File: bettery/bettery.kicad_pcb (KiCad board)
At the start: 2 copper layers, 72.2 x 45.2 mm, 61 parts, among them J2 Conn_01x10_Socket, J4 Conn_ARM_SWD_TagConnect_TC2030, Q1 WMB014N06LG4, Q2 WMB014N06LG4, U1 L9961, U2 STM32G070KBTx

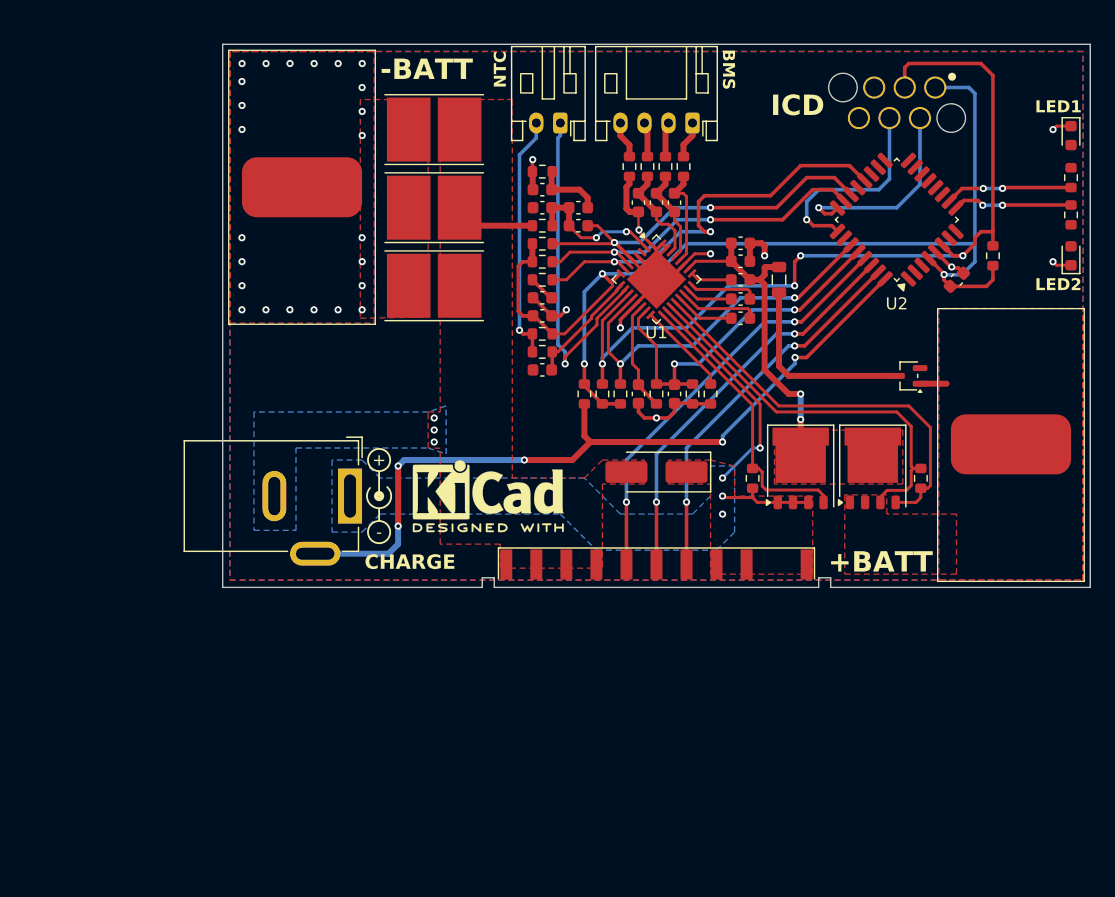
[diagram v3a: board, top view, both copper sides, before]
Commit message: add chassis models
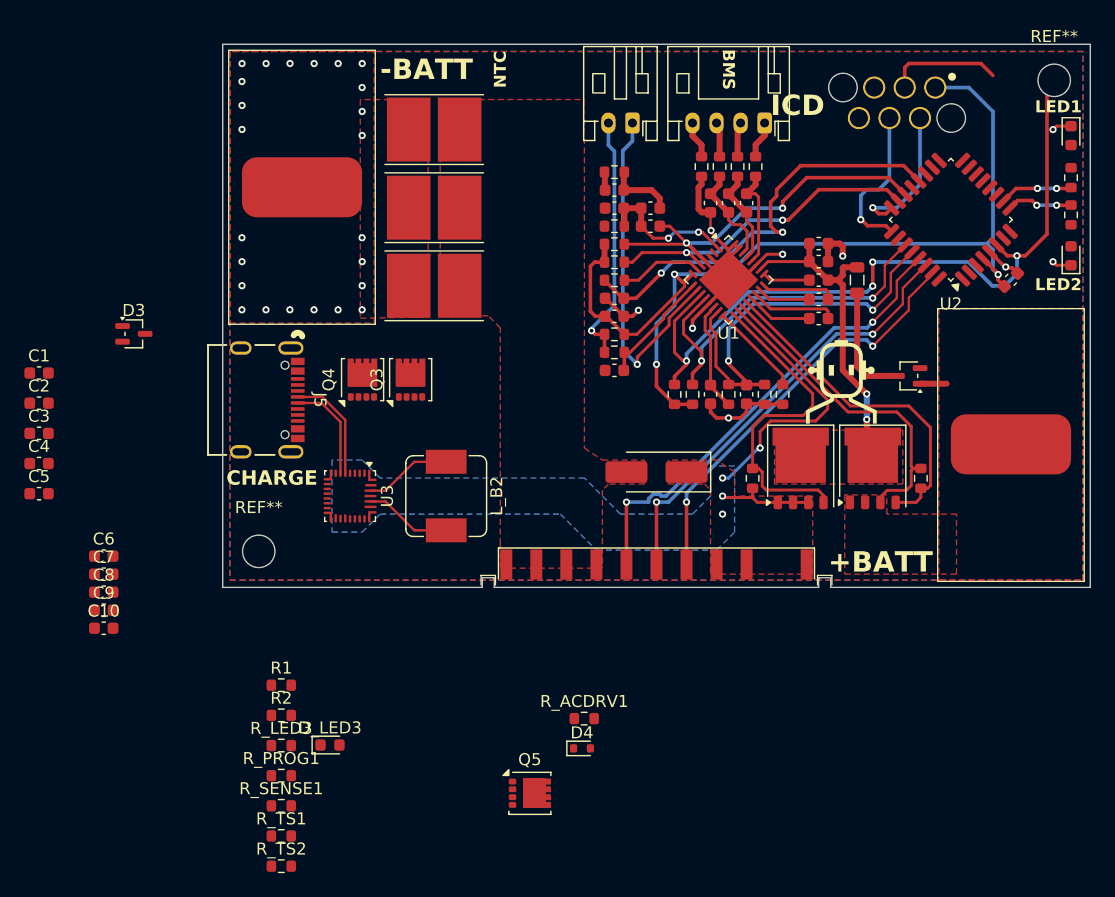
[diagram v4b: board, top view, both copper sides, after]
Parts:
- removed J_CHG1: Barrel_Jack_Switch, Connector_BarrelJack:BarrelJack_GCT_DCJ200-10-A_Horizontal
- removed the REF** at (86.0, 115.0)
- removed the REF** at (76.8, 115.0)
- removed R_PU2, R_PU3: 10k, Resistor_SMD:R_0603_1608Metric
- added C1: 4.7n, Capacitor_SMD:C_0603_1608Metric, F.Cu at (48.6, 104.8)
- added C10: 10u, Capacitor_SMD:C_0603_1608Metric, F.Cu at (54.0, 126.0)
- added C2: 4.7n, Capacitor_SMD:C_0603_1608Metric, F.Cu at (48.6, 107.3)
- added C3: 4.7u, Capacitor_SMD:C_0603_1608Metric, F.Cu at (48.6, 109.8)
- added C4: 10u, Capacitor_SMD:C_0603_1608Metric, F.Cu at (48.6, 112.3)
- added C5: 10u, Capacitor_SMD:C_0603_1608Metric, F.Cu at (48.6, 114.8)
- added C6: 10u, Capacitor_SMD:C_0603_1608Metric, F.Cu at (54.0, 120.0)
- added C7: 10u, Capacitor_SMD:C_0603_1608Metric, F.Cu at (54.0, 121.5)
- added C8: 10u, Capacitor_SMD:C_0603_1608Metric, F.Cu at (54.0, 123.0)
- added C9: 10u, Capacitor_SMD:C_0603_1608Metric, F.Cu at (54.0, 124.5)
- added D3: BAT54SWFILMY, Package_TO_SOT_SMD:SOT-323_SC-70, F.Cu at (56.5, 101.5)
- added D4: BZT52C12T-7, Diode_SMD:D_SOD-523, F.Cu at (93.8, 136.0)
- added D_LED3: LED, LED_SMD:LED_0603_1608Metric, F.Cu at (72.8, 135.7)
- added J5: CONN12_RAHUC31_SWC, bettery:CONN12_RAHUC31_SWC, F.Cu at (66.5, 107.0)
- added L_B2: 1u, Inductor_SMD:L_Sumida_CDMC6D28_7.25x6.5mm, F.Cu at (82.5, 115.0)
- added Q3: CSD17575Q3, Package_SON:VSON-8_3.3x3.3mm_P0.65mm_NexFET, F.Cu at (79.5, 105.3)
- added Q4: CSD17581Q3A, Package_SON:VSON-8_3.3x3.3mm_P0.65mm_NexFET, F.Cu at (75.5, 105.3)
- added Q5: CSD17581Q3A, Package_SON:VSON-8_3.3x3.3mm_P0.65mm_NexFET, F.Cu at (89.5, 139.7)
- added R1: 10.5k, Resistor_SMD:R_0603_1608Metric, F.Cu at (68.8, 130.7)
- added R2: 10.5k, Resistor_SMD:R_0603_1608Metric, F.Cu at (68.8, 133.2)
- added REF**: MountingHole_2.7mm_M2.5, MountingHole:MountingHole_2.7mm_M2.5, F.Cu at (66.9, 119.6)
- added REF**: MountingHole_2.7mm_M2.5, MountingHole:MountingHole_2.7mm_M2.5, F.Cu at (133.1, 80.4)
- added REF**: Beta-LOGO-3, BETA:Beta-LOGO-3, F.Cu at (115.4, 106.1)
- added R_ACDRV1: 294, Resistor_SMD:R_0603_1608Metric, F.Cu at (94.0, 133.5)
- added R_LED3: 2.2k, Resistor_SMD:R_0603_1608Metric, F.Cu at (68.8, 135.8)
- added R_PROG1: 10.5k, Resistor_SMD:R_0603_1608Metric, F.Cu at (68.8, 138.3)
- added R_SENSE1: 100, Resistor_SMD:R_0603_1608Metric, F.Cu at (68.8, 140.8)
- added R_TS1: 10.5k, Resistor_SMD:R_0603_1608Metric, F.Cu at (68.8, 143.3)
- added R_TS2: 10.5k, Resistor_SMD:R_0603_1608Metric, F.Cu at (68.8, 145.8)
- added U3: BQ25798, Package_DFN_QFN:Texas_RQM0029A_VQFN-29_4x4mm_P0.4mm, F.Cu at (74.5, 115.0)
- R_LED1, R_LED2: value 10k -> 2.2k
- moved C_B1 6.50 mm to (113.5, 94.0)
- moved C_B2 6.50 mm to (113.5, 95.5)
- moved C_CP1 6.50 mm to (113.5, 97.0)
- moved C_CP_1 6.50 mm to (113.5, 100.2)
- moved C_CP_2 6.50 mm to (113.5, 98.6)
- moved L_B1 6.50 mm to (116.7, 97.0)
- moved C_FILL1 6.00 mm to (96.5, 104.5)
- moved C_ISENSE_1 6.00 mm to (99.5, 92.5)
- moved C_ISENSE_2 6.00 mm to (99.5, 91.0)
- moved C_ISENSE_CM1 6.00 mm to (96.5, 89.5)
- moved C_ISENSE_CM2 6.00 mm to (96.5, 91.0)
- moved C_LPF1 6.00 mm to (104.5, 90.6)
- moved C_LPF2 6.00 mm to (106.0, 90.6)
- moved C_LPF3 6.00 mm to (107.5, 90.6)
- moved C_NSHIP1 6.00 mm to (107.5, 106.5)
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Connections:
- C_ISENSE_1 pad 2: /ISENSEP -> /ISENSEM
- C_ISENSE_2 pad 2: /ISENSEP -> /ISENSEM
- C_ISENSE_CM2 pad 1: /ISENSEP -> /ISENSEM
- C_RDY1 pad 1: Net-(C_RDY1-Pad1) -> /RDY
- C_VREG1 pad 1: /VREG -> +3.3V
- J4 pad 3: /FAULTN_SAFE -> /NRST
- R_FLTS_UP1 pad 1: /FAULTN_SAFE -> +3.3V
- R_FLTS_UP1 pad 2: /VREG -> /FAULTN_SAFE
- R_FLT_UP1 pad 2: /VREG -> +3.3V
- R_ISENSE2 pad 1: /ISENSEP -> /ISENSEM
- R_PU1 pad 1: /VREG -> +3.3V
- R_RDY1 pad 1: Net-(C_RDY1-Pad1) -> /RDY
- R_RDY1 pad 2: /RDY -> Net-(U1-RDY)
- R_SCL_UP1 pad 2: /VREG -> +3.3V
- R_SDA_UP1 pad 2: /VREG -> +3.3V
- U1 pad 2: /ISENSEP -> /ISENSEM
- U1 pad 5: /SCL -> /I2C2_SCL
- U1 pad 6: /SDA -> /I2C2_SDA
- U1 pad 7: /RDY -> Net-(U1-RDY)
- U1 pad 8: /VREG -> +3.3V
- U2 pad 22: /SCL -> /I2C2_SCL
- U2 pad 23: /SDA -> /I2C2_SDA
- U2 pad 32: /CHG_SIG -> unconnected-(U2-PB8-Pad32)
- U2 pad 4: /VREG -> +3.3V
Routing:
- net /CHG_SIG: track 64.7 -> 0.00 mm, vias 5 -> 0
- net /VREG: track 93.5 -> 80.5 mm
- net /ISENSEM: track 11.7 -> 23.8 mm, vias 0 -> 2
- net /ISENSEP: track 12.1 -> 0.00 mm, vias 2 -> 0
- net /FAULTN_SAFE: track 73.1 -> 63.1 mm
- net /NRST: track 0.00 -> 9.56 mm
- net Net-(U3-D+): track 0.00 -> 9.18 mm
- net Net-(U3-D-): track 0.00 -> 8.48 mm
- net Net-(U3-SW2): track 0.00 -> 7.29 mm
- net Net-(U3-SW1): track 0.00 -> 7.29 mm
- net Net-(U1-RDY): track 0.00 -> 6.95 mm
- net -PACK: track 6.68 -> 0.00 mm, vias 3 -> 0
- net Net-(D1A-K): track 16.3 -> 9.82 mm
- net /CHG: track 34.2 -> 28.2 mm
- net +BATT: track 35.5 -> 29.4 mm
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- removed copper zone on B.Cu, net -PACK
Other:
- board text added: "FAN"
- board text removed: "+"
- board text removed: "-"
